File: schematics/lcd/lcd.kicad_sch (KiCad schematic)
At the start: 27 parts, among them J1 JST_01x06, Q1 BSS138, Q2 BSS138, Q3 BSS138, Q4 BSS138, U1 NHD-C12832A1Z, U2 TLV70033_SOT23-5

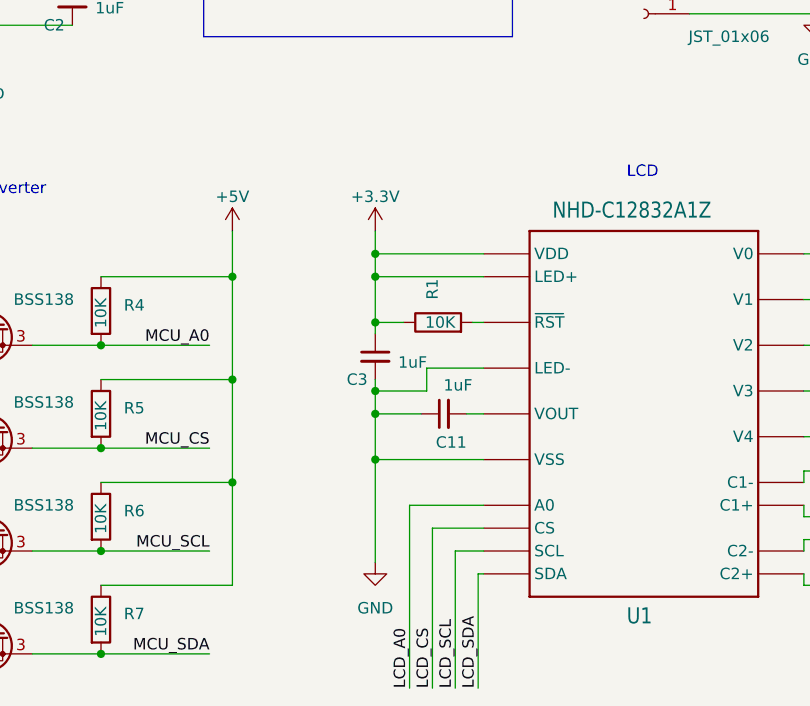
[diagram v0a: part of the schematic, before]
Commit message: SCH: LCD=> add pot for backlight brightness
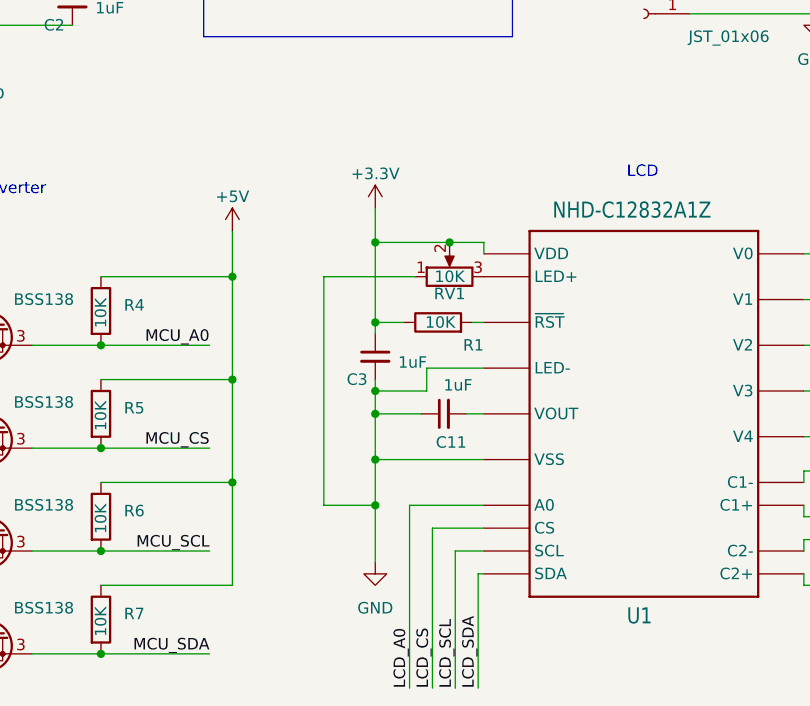
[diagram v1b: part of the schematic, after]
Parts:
- added RV1: 10K, Potentiometer_SMD:Potentiometer_Bourns_3314G_Vertical, symbol Device:R_Potentiometer
- U1: JLCPCB BOM (none) -> 0
- U2: LCSC C2871194 -> (none); lscs (none) -> C2871194
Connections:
- net +3.3V: now also RV1.2; no longer U1.P18 (LED+)
- net GND: now also RV1.1
- new net: RV1.3, U1.P18 (LED+)
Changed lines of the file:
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@@
   (junction (at 100.33 76.835) (diameter 0) (color 0 0 0 0)
   )
-  (junction (at 143.51 102.235) (diameter 0) (color 0 0 0 0)
-  )
   (junction (at 113.03 146.685) (diameter 0) (color 0 0 0 0)
   )
   (junction (at 207.01 107.315) (diameter 0) (color 0 0 0 0)
   )
-  (junction (at 143.51 104.775) (diameter 0) (color 0 0 0 0)
-  )
   (junction (at 86.36 146.685) (diameter 0) (color 0 0 0 0)
   )
@@
   (junction (at 92.71 62.23) (diameter 0) (color 0 0 0 0)
   )
+  (junction (at 143.51 130.175) (diameter 0) (color 0 0 0 0)
+  )
   (junction (at 127.635 127.635) (diameter 0) (color 0 0 0 0)
   )
   (junction (at 71.755 116.205) (diameter 0) (color 0 0 0 0)
   )
+  (junction (at 143.51 100.965) (diameter 0) (color 0 0 0 0)
+  )
   (junction (at 86.36 123.825) (diameter 0) (color 0 0 0 0)
   )
@@
   (junction (at 86.36 112.395) (diameter 0) (color 0 0 0 0)
   )
+  (junction (at 151.765 100.965) (diameter 0) (color 0 0 0 0)
+  )
   (wire (pts (xy 86.36 123.825) (xy 95.25 123.825))
     (stroke (width 0) (type default))
@@
     (stroke (width 0) (type default))
   )
+  (wire (pts (xy 155.575 102.235) (xy 155.575 100.965))
+    (stroke (width 0) (type default))
+  )
   (wire (pts (xy 86.36 104.775) (xy 100.33 104.775))
     (stroke (width 0) (type default))
@@
     (stroke (width 0) (type default))
   )
+  (wire (pts (xy 143.51 130.175) (xy 143.51 136.525))
+    (stroke (width 0) (type default))
+  )
   (wire (pts (xy 113.03 135.255) (xy 125.095 135.255))
     (stroke (width 0) (type default))
@@
     (stroke (width 0) (type default))
   )
-  (wire (pts (xy 143.51 125.095) (xy 143.51 136.525))
-    (stroke (width 0) (type default))
-  )
-  (wire (pts (xy 143.51 102.235) (xy 143.51 99.695))
+  (wire (pts (xy 143.51 125.095) (xy 143.51 130.175))
     (stroke (width 0) (type default))
   )
@@
     (stroke (width 0) (type default))
   )
+  (wire (pts (xy 137.795 130.175) (xy 143.51 130.175))
+    (stroke (width 0) (type default))
+  )
   (wire (pts (xy 86.36 116.205) (xy 100.33 116.205))
     (stroke (width 0) (type default))
@@
     (stroke (width 0) (type default))
   )
+  (wire (pts (xy 151.765 100.965) (xy 143.51 100.965))
+    (stroke (width 0) (type default))
+  )
   (wire (pts (xy 74.93 123.825) (xy 86.36 123.825))
     (stroke (width 0) (type default))
@@
     (stroke (width 0) (type default))
   )
-  (wire (pts (xy 143.51 104.775) (xy 143.51 109.855))
+  (wire (pts (xy 143.51 97.155) (xy 143.51 100.965))
     (stroke (width 0) (type default))
   )
@@
     (stroke (width 0) (type default))
   )
+  (wire (pts (xy 155.575 100.965) (xy 151.765 100.965))
+    (stroke (width 0) (type default))
+  )
   (wire (pts (xy 143.51 125.095) (xy 155.575 125.095))
     (stroke (width 0) (type default))
@@
     (stroke (width 0) (type default))
   )
-  (wire (pts (xy 143.51 102.235) (xy 143.51 104.775))
+  (wire (pts (xy 137.795 104.775) (xy 137.795 130.175))
     (stroke (width 0) (type default))
   )
@@
     (stroke (width 0) (type default))
   )
+  (wire (pts (xy 147.955 104.775) (xy 137.795 104.775))
+    (stroke (width 0) (type default))
+  )
   (wire (pts (xy 191.135 133.985) (xy 194.945 133.985))
     (stroke (width 0) (type default))
@@
     (stroke (width 0) (type default))
   )
+  (wire (pts (xy 143.51 100.965) (xy 143.51 109.855))
+    (stroke (width 0) (type default))
+  )
   (wire (pts (xy 191.135 126.365) (xy 191.135 127.635))
     (stroke (width 0) (type default))
@@
     (stroke (width 0) (type default))
   )
-  (wire (pts (xy 155.575 102.235) (xy 143.51 102.235))
-    (stroke (width 0) (type default))
-  )
   (wire (pts (xy 207.01 112.395) (xy 207.01 117.475))
     (stroke (width 0) (type default))
@@
   )
   (wire (pts (xy 105.41 112.395) (xy 113.03 112.395))
-    (stroke (width 0) (type default))
-  )
-  (wire (pts (xy 143.51 104.775) (xy 155.575 104.775))
     (stroke (width 0) (type default))
   )
@@
       (effects (font (size 1.27 1.27)) hide)
     )
-    (property "LCSC" "C2871194" (at 100.33 64.77 0)
+    (property "lscs" "C2871194" (at 100.33 64.77 0)
       (effects (font (size 1.27 1.27)) hide)
     )
@@
     )
     (property "Datasheet" "" (at 173.355 120.015 0)
+      (effects (font (size 1.27 1.27)) hide)
+    )
+    (property "JLCPCB BOM" "0" (at 173.355 120.015 0)
       (effects (font (size 1.27 1.27)) hide)
     )
@@
   (symbol (lib_id "Device:R") (at 150.495 109.855 90) (unit 1)
     (in_bom yes) (on_board yes) (dnp no)
-    (property "Reference" "R1" (at 149.86 107.315 0)
+    (property "Reference" "R1" (at 155.575 112.395 90)
       (effects (font (size 1.27 1.27)) (justify left))
     )
@@
         (path "/3da7706e-8391-4331-ba0b-48fd1cd1300f"
           (reference "C6") (unit 1)
+        )
+      )
+    )
+  )
+  (symbol (lib_id "Device:R_Potentiometer") (at 151.765 104.775 90) (unit 1)
+    (in_bom yes) (on_board yes) (dnp no)
+    (property "Reference" "RV1" (at 151.765 106.68 90)
+      (effects (font (size 1.27 1.27)))
+    )
+    (property "Value" "10K" (at 151.765 104.775 90)
+      (effects (font (size 1.27 1.27)))
+    )
+    (property "Footprint" "Potentiometer_SMD:Potentiometer_Bourns_3314G_Vertical" (at 151.765 104.775 0)
+      (effects (font (size 1.27 1.27)) hide)
+    )
+    (property "Datasheet" "~" (at 151.765 104.775 0)
+      (effects (font (size 1.27 1.27)) hide)
+    )
+    (property "lcsc" "C780220" (at 151.765 104.775 90)
+      (effects (font (size 1.27 1.27)) hide)
+    )
+    (pin "1")
+    (pin "2")
+    (pin "3")
+    (instances
+      (project "lcd"
+        (path "/3da7706e-8391-4331-ba0b-48fd1cd1300f"
+          (reference "RV1") (unit 1)
         )
       )
@@
     )
   )
-  (symbol (lib_id "power:+3.3V") (at 143.51 99.695 0) (unit 1)
+  (symbol (lib_id "power:+3.3V") (at 143.51 97.155 0) (unit 1)
     (in_bom yes) (on_board yes) (dnp no) (fields_autoplaced)
-    (property "Reference" "#PWR04" (at 143.51 103.505 0)
-      (effects (font (size 1.27 1.27)) hide)
-    )
-    (property "Value" "+3.3V" (at 143.51 95.885 0)
-      (effects (font (size 1.27 1.27)))
-    )
-    (property "Footprint" "" (at 143.51 99.695 0)
-      (effects (font (size 1.27 1.27)) hide)
-    )
-    (property "Datasheet" "" (at 143.51 99.695 0)
-      (effects (font (size 1.27 1.27)) hide)
-    )
+    (property "Reference" "#PWR04" (at 143.51 100.965 0)
+      (effects (font (size 1.27 1.27)) hide)
+    )
+    (property "Value" "+3.3V" (at 143.51 93.345 0)
+      (effects (font (size 1.27 1.27)))
+    )
+    (property "Footprint" "" (at 143.51 97.155 0)
+      (effects (font (size 1.27 1.27)) hide)
+    )
+    (property "Datasheet" "" (at 143.51 97.155 0)
+      (effects (font (size 1.27 1.27)) hide)
+    )

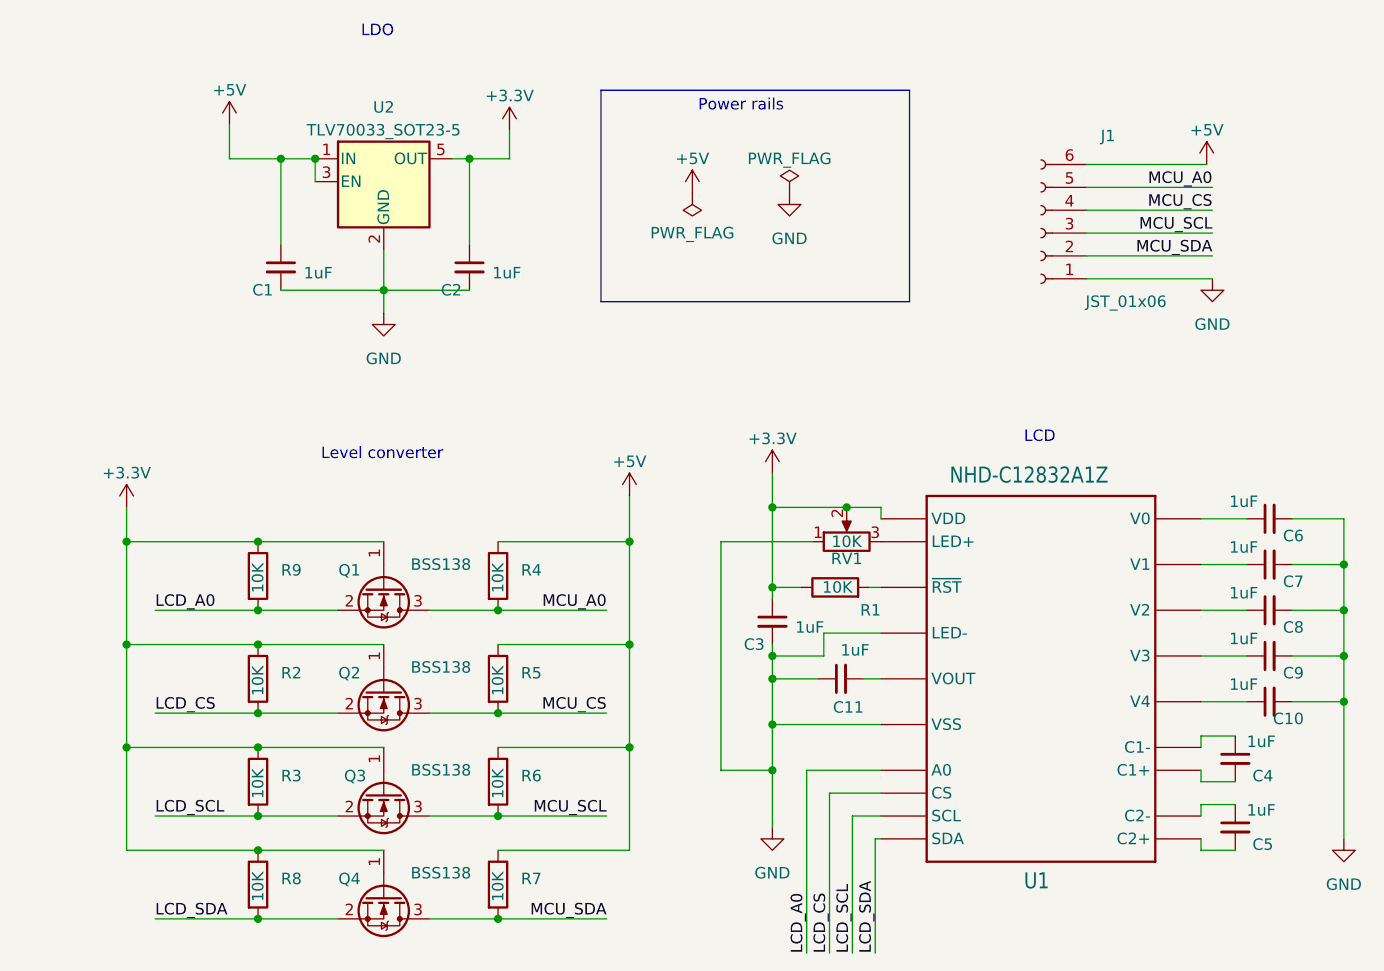
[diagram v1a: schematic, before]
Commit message: SCH: LCD=> Changed level shifter
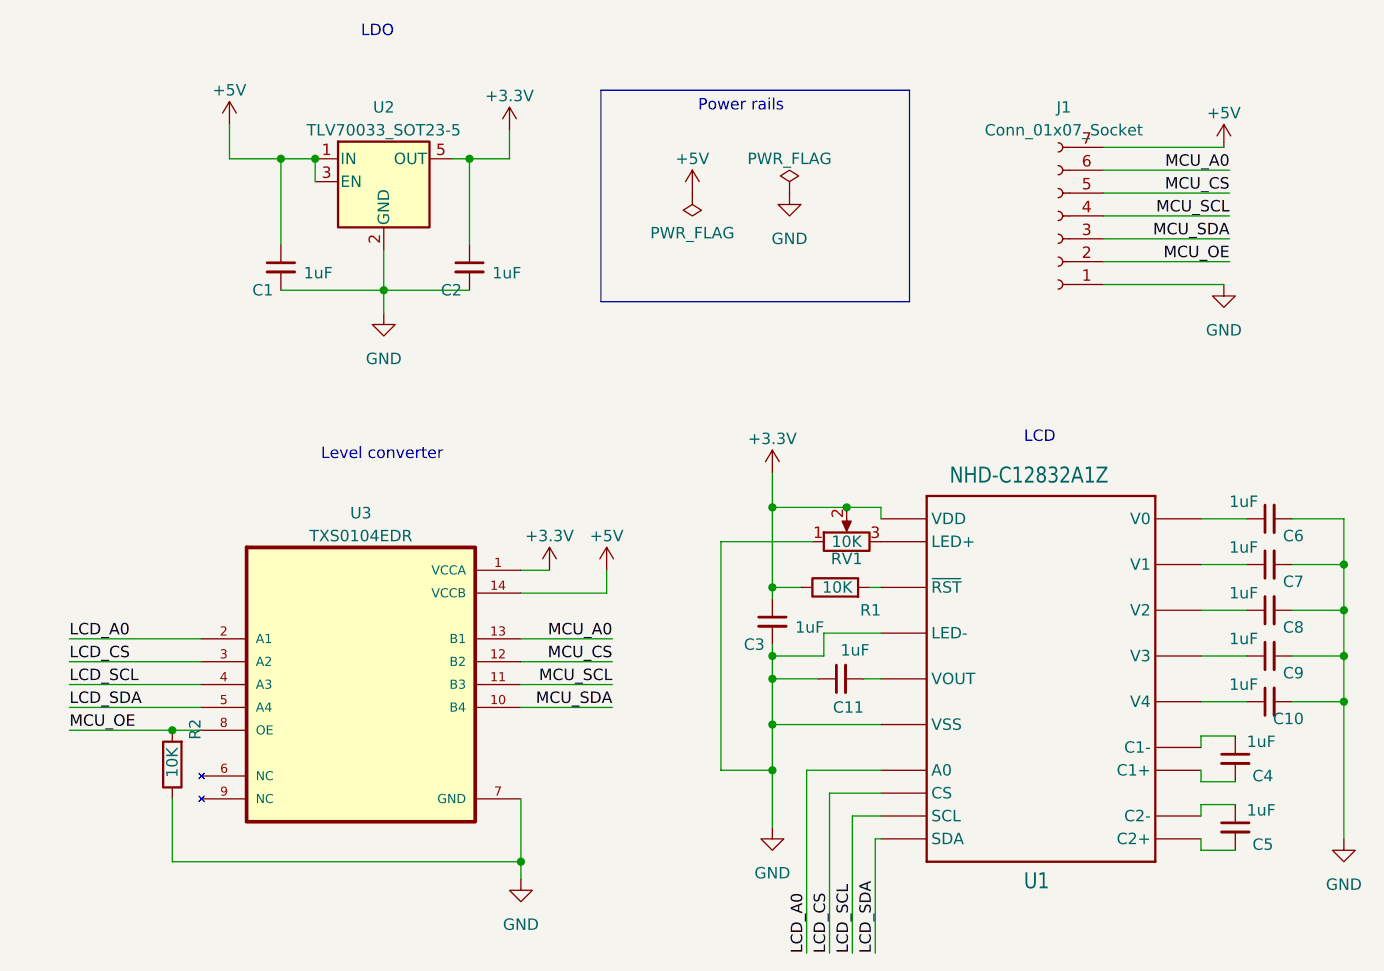
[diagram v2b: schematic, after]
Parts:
- removed J1: JST_01x06, Connector_JST:JST_PH_B6B-PH-K_1x06_P2.00mm_Vertical, symbol Connector:Conn_01x06_Socket
- removed Q1, Q2, Q3, Q4: BSS138, Package_TO_SOT_SMD:SOT-23, symbol Transistor_FET:BSS138
- removed R3, R4, R5, R6, R7, R8, R9: 10K, Resistor_SMD:R_0603_1608Metric, symbol Device:R
- added J1: Conn_01x07_Socket, Connector_JST:JST_PH_B7B-PH-K_1x07_P2.00mm_Vertical, symbol Connector:Conn_01x07_Socket
- added U3: TXS0104EDR, library:SOIC127P600X175-14N, symbol TXS0104EDR:TXS0104EDR
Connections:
- net +3.3V: now also U3.1 (VCCA); no longer R2.1
- net +5V: now also J1.7 (Pin_7), U3.14 (VCCB)
- net GND: now also R2.1, J1.1 (Pin_1), U3.7 (GND)
- net LCD_A0: now also U3.2 (A1)
- net LCD_CS: now also U3.3 (A2); no longer R2.2
- net LCD_SCL: now also U3.4 (A3)
- net LCD_SDA: now also U3.5 (A4)
- net MCU_A0: now also J1.6 (Pin_6), U3.13 (B1)
- net MCU_CS: now also J1.5 (Pin_5), U3.12 (B2)
- net MCU_SCL: now also J1.4 (Pin_4), U3.11 (B3)
- net MCU_SDA: now also J1.3 (Pin_3), U3.10 (B4)
- new net MCU_OE: J1.2 (Pin_2), R2.2, U3.8 (OE)
